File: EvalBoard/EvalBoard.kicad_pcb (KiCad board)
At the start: 2 copper layers, 75 x 35 mm, 19 parts, among them J1 Conn_01x01, J10 Conn_01x01, J11 Conn_01x02, J12 Conn_01x05, J2 Conn_01x01, J4 Conn_01x01, J5 Conn_01x01, J6 Conn_01x01, J7 Conn_01x01, J8 Conn_01x01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

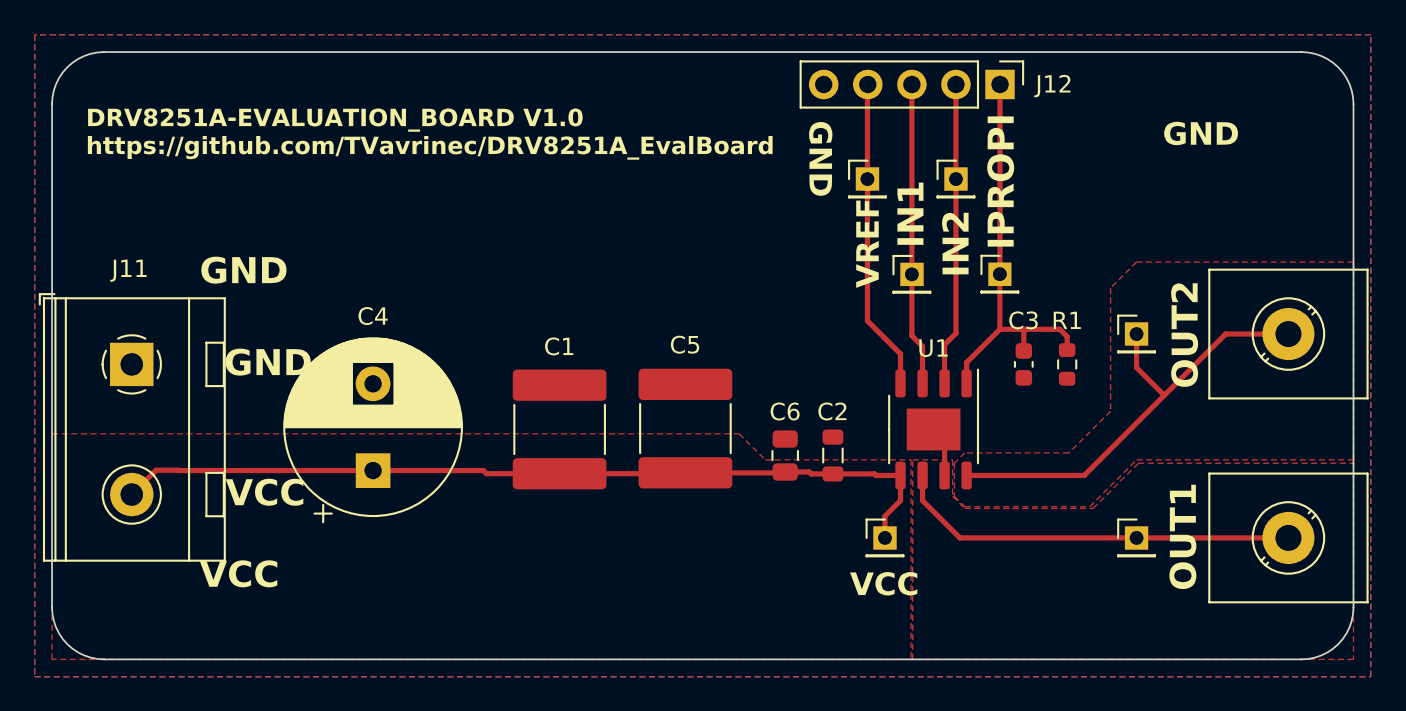
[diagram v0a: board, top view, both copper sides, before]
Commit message: Mounting holes and ground vias
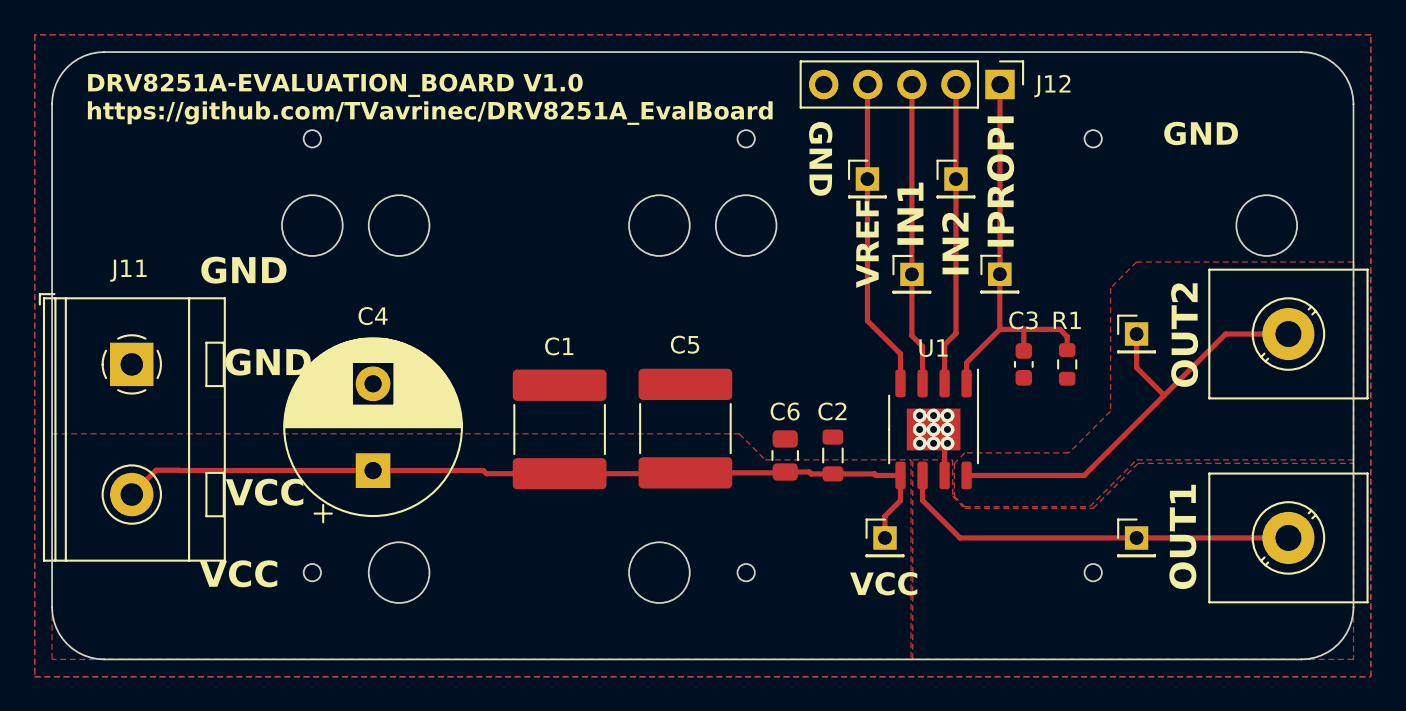
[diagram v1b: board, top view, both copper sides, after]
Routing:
- net GND: track 2.91 -> 3.73 mm, vias 0 -> 9
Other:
- outline, holes or cut-outs redrawn
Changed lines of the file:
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@@
     )
   )
+  (gr_circle (center 125 95) (end 125.5 95)
+    (stroke (width 0.1) (type default)) (fill none) (layer "Edge.Cuts"))
+  (gr_circle (center 145 75) (end 146.75 75)
+    (stroke (width 0.1) (type default)) (fill none) (layer "Edge.Cuts"))
   (gr_line (start 185 68) (end 185 97)
     (stroke (width 0.1) (type default)) (layer "Edge.Cuts"))
@@
   (gr_arc (start 110 68) (mid 110.87868 65.87868) (end 113 65)
     (stroke (width 0.1) (type default)) (layer "Edge.Cuts"))
+  (gr_circle (center 125 75) (end 126.75 75)
+    (stroke (width 0.1) (type default)) (fill none) (layer "Edge.Cuts"))
+  (gr_circle (center 130 95) (end 131.75 95)
+    (stroke (width 0.1) (type default)) (fill none) (layer "Edge.Cuts"))
+  (gr_circle (center 150 75) (end 151.75 75)
+    (stroke (width 0.1) (type default)) (fill none) (layer "Edge.Cuts"))
   (gr_line (start 182 100) (end 113 100)
     (stroke (width 0.1) (type default)) (layer "Edge.Cuts"))
+  (gr_circle (center 145 95) (end 146.75 95)
+    (stroke (width 0.1) (type default)) (fill none) (layer "Edge.Cuts"))
+  (gr_circle (center 130 75) (end 131.75 75)
+    (stroke (width 0.1) (type default)) (fill none) (layer "Edge.Cuts"))
   (gr_line (start 110 97) (end 110 68)
     (stroke (width 0.1) (type default)) (layer "Edge.Cuts"))
+  (gr_circle (center 170 95) (end 170.5 95)
+    (stroke (width 0.1) (type default)) (fill none) (layer "Edge.Cuts"))
+  (gr_circle (center 150 95) (end 150.5 95)
+    (stroke (width 0.1) (type default)) (fill none) (layer "Edge.Cuts"))
+  (gr_circle (center 180 75) (end 181.75 75)
+    (stroke (width 0.1) (type default)) (fill none) (layer "Edge.Cuts"))
   (gr_arc (start 182 65) (mid 184.12132 65.87868) (end 185 68)
     (stroke (width 0.1) (type default)) (layer "Edge.Cuts"))
   (gr_arc (start 113 100) (mid 110.87868 99.12132) (end 110 97)
     (stroke (width 0.1) (type default)) (layer "Edge.Cuts"))
+  (gr_circle (center 125 70) (end 125.5 70)
+    (stroke (width 0.1) (type default)) (fill none) (layer "Edge.Cuts"))
   (gr_line (start 113 65) (end 182 65)
     (stroke (width 0.1) (type default)) (layer "Edge.Cuts"))
+  (gr_circle (center 150 70) (end 150.5 70)
+    (stroke (width 0.1) (type default)) (fill none) (layer "Edge.Cuts"))
+  (gr_circle (center 170 70) (end 170.5 70)
+    (stroke (width 0.1) (type default)) (fill none) (layer "Edge.Cuts"))
   (gr_text "GND" (at 155.15 68.94 -270) (layer "B.SilkS")
     (effects (font (size 1.3 1.3) (thickness 0.3) bold) (justify left bottom mirror))
   )
-  (gr_text "DRV8251A-EVALUATION_BOARD V1.0\nhttps://github.com/TVavrinec/DRV8251A_EvalBoard" (at 151.51 71) (layer "B.SilkS")
+  (gr_text "DRV8251A-EVALUATION_BOARD V1.0\nhttps://github.com/TVavrinec/DRV8251A_EvalBoard" (at 151.51 69) (layer "B.SilkS")
     (effects (font (size 1 1) (thickness 0.2) bold) (justify left bottom mirror))
   )
@@
     (effects (font (size 1.5 1.5) (thickness 0.3) bold) (justify left bottom))
   )
-  (gr_text "DRV8251A-EVALUATION_BOARD V1.0\nhttps://github.com/TVavrinec/DRV8251A_EvalBoard" (at 111.95 71) (layer "F.SilkS")
+  (gr_text "DRV8251A-EVALUATION_BOARD V1.0\nhttps://github.com/TVavrinec/DRV8251A_EvalBoard" (at 111.95 69) (layer "F.SilkS")
     (effects (font (size 1 1) (thickness 0.2) bold) (justify left bottom))
   )
@@
     (effects (font (size 1.5 1.5) (thickness 0.3) bold) (justify left bottom))
   )
-  (segment (start 161.435 89.4) (end 161.435 87.385) (width 0.3) (layer "F.Cu") (net 1))
-  (segment (start 161.435 87.385) (end 160.8 86.75) (width 0.3) (layer "F.Cu") (net 1))
+  (segment (start 161.55 87.5) (end 160.8 87.5) (width 0.3) (layer "F.Cu") (net 1))
+  (segment (start 161.435 87.565) (end 161.5 87.5) (width 0.3) (layer "F.Cu") (net 1))
+  (segment (start 160.8 86.8) (end 160.8 86.75) (width 0.3) (layer "F.Cu") (net 1))
+  (segment (start 161.435 87.435) (end 161.435 87.385) (width 0.3) (layer "F.Cu") (net 1))
+  (segment (start 161.435 89.4) (end 161.435 87.565) (width 0.3) (layer "F.Cu") (net 1))
+  (segment (start 161.435 87.385) (end 161.55 87.5) (width 0.3) (layer "F.Cu") (net 1))
+  (segment (start 160.8 87.5) (end 160.8 86.8) (width 0.3) (layer "F.Cu") (net 1))
+  (segment (start 161.5 87.5) (end 161.435 87.435) (width 0.3) (layer "F.Cu") (net 1))
+  (segment (start 160.8 86.75) (end 160.8 86.75) (width 0.3) (layer "F.Cu") (net 1))
+  (via (at 160.8 87.55) (size 0.8) (drill 0.4) (layers "F.Cu" "B.Cu") (net 1))
+  (via (at 160.8 86.75) (size 0.8) (drill 0.4) (layers "F.Cu" "B.Cu") (net 1))
+  (via (at 161.6 86.75) (size 0.8) (drill 0.4) (layers "F.Cu" "B.Cu") (net 1))
+  (via (at 161.6 85.95) (size 0.8) (drill 0.4) (layers "F.Cu" "B.Cu") (net 1))
+  (via (at 161.6 87.55) (size 0.8) (drill 0.4) (layers "F.Cu" "B.Cu") (net 1))
+  (via (at 160.8 85.95) (size 0.8) (drill 0.4) (layers "F.Cu" "B.Cu") (net 1))
+  (via (at 160 86.75) (size 0.8) (drill 0.4) (layers "F.Cu" "B.Cu") (net 1))
+  (via (at 160 87.55) (size 0.8) (drill 0.4) (layers "F.Cu" "B.Cu") (net 1))
+  (via (at 160 85.95) (size 0.8) (drill 0.4) (layers "F.Cu" "B.Cu") (net 1))
   (segment (start 134.857677 89.117677) (end 135.04 89.3) (width 0.3) (layer "F.Cu") (net 2))
   (segment (start 157.49 89.4) (end 158.895 89.4) (width 0.3) (layer "F.Cu") (net 2))

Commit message: Margine around mounting holes
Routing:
- net GND: vias 9 -> 15
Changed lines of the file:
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@@
   (gr_circle (center 170 70) (end 170.5 70)
     (stroke (width 0.1) (type default)) (fill none) (layer "Edge.Cuts"))
+  (gr_circle (center 170 95) (end 171.25 95)
+    (stroke (width 0.15) (type default)) (fill none) (layer "Margin"))
+  (gr_circle (center 150 75) (end 146.5 75.5)
+    (stroke (width 0.15) (type default)) (fill none) (layer "Margin"))
+  (gr_circle (center 130 75) (end 126.5 75.5)
+    (stroke (width 0.15) (type default)) (fill none) (layer "Margin"))
+  (gr_circle (center 130 95) (end 126.5 95.5)
+    (stroke (width 0.15) (type default)) (fill none) (layer "Margin"))
+  (gr_circle (center 125 70) (end 126.25 70)
+    (stroke (width 0.15) (type default)) (fill none) (layer "Margin"))
+  (gr_circle (center 145 95) (end 141.5 95.5)
+    (stroke (width 0.15) (type default)) (fill none) (layer "Margin"))
+  (gr_circle (center 180 75) (end 176.5 75.5)
+    (stroke (width 0.15) (type default)) (fill none) (layer "Margin"))
+  (gr_circle (center 125 95) (end 126.25 95)
+    (stroke (width 0.15) (type default)) (fill none) (layer "Margin"))
+  (gr_circle (center 125 75) (end 121.5 75.5)
+    (stroke (width 0.15) (type default)) (fill none) (layer "Margin"))
+  (gr_circle (center 150 70) (end 151.25 70)
+    (stroke (width 0.15) (type default)) (fill none) (layer "Margin"))
+  (gr_circle (center 170 70) (end 171.25 70)
+    (stroke (width 0.15) (type default)) (fill none) (layer "Margin"))
+  (gr_circle (center 145 75) (end 141.5 75.5)
+    (stroke (width 0.15) (type default)) (fill none) (layer "Margin"))
+  (gr_circle (center 150 95) (end 151.25 95)
+    (stroke (width 0.15) (type default)) (fill none) (layer "Margin"))
   (gr_text "GND" (at 155.15 68.94 -270) (layer "B.SilkS")
     (effects (font (size 1.3 1.3) (thickness 0.3) bold) (justify left bottom mirror))
@@
     (effects (font (size 1.5 1.5) (thickness 0.3) bold) (justify left bottom))
   )
-  (gr_text "GND" (at 174 70.5) (layer "F.SilkS")
+  (gr_text "GND" (at 173.9 70.7) (layer "F.SilkS")
     (effects (font (size 1.3 1.3) (thickness 0.3) bold) (justify left bottom))
   )
@@
   (via (at 160.8 87.55) (size 0.8) (drill 0.4) (layers "F.Cu" "B.Cu") (net 1))
   (via (at 160.8 86.75) (size 0.8) (drill 0.4) (layers "F.Cu" "B.Cu") (net 1))
+  (via (at 179.59 68.5) (size 0.8) (drill 0.4) (layers "F.Cu" "B.Cu") (free) (net 1))
   (via (at 161.6 86.75) (size 0.8) (drill 0.4) (layers "F.Cu" "B.Cu") (net 1))
   (via (at 161.6 85.95) (size 0.8) (drill 0.4) (layers "F.Cu" "B.Cu") (net 1))
   (via (at 161.6 87.55) (size 0.8) (drill 0.4) (layers "F.Cu" "B.Cu") (net 1))
+  (via (at 173.86 68.5) (size 0.8) (drill 0.4) (layers "F.Cu" "B.Cu") (free) (net 1))
+  (via (at 181.5 68.5) (size 0.8) (drill 0.4) (layers "F.Cu" "B.Cu") (free) (net 1))
   (via (at 160.8 85.95) (size 0.8) (drill 0.4) (layers "F.Cu" "B.Cu") (net 1))
+  (via (at 175.77 68.5) (size 0.8) (drill 0.4) (layers "F.Cu" "B.Cu") (free) (net 1))
+  (via (at 177.68 68.5) (size 0.8) (drill 0.4) (layers "F.Cu" "B.Cu") (free) (net 1))
   (via (at 160 86.75) (size 0.8) (drill 0.4) (layers "F.Cu" "B.Cu") (net 1))
   (via (at 160 87.55) (size 0.8) (drill 0.4) (layers "F.Cu" "B.Cu") (net 1))
+  (via (at 171.95 68.5) (size 0.8) (drill 0.4) (layers "F.Cu" "B.Cu") (free) (net 1))
   (via (at 160 85.95) (size 0.8) (drill 0.4) (layers "F.Cu" "B.Cu") (net 1))
   (segment (start 134.857677 89.117677) (end 135.04 89.3) (width 0.3) (layer "F.Cu") (net 2))
